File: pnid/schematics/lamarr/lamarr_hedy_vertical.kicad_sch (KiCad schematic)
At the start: 103 parts, among them U1 Rocket_Big

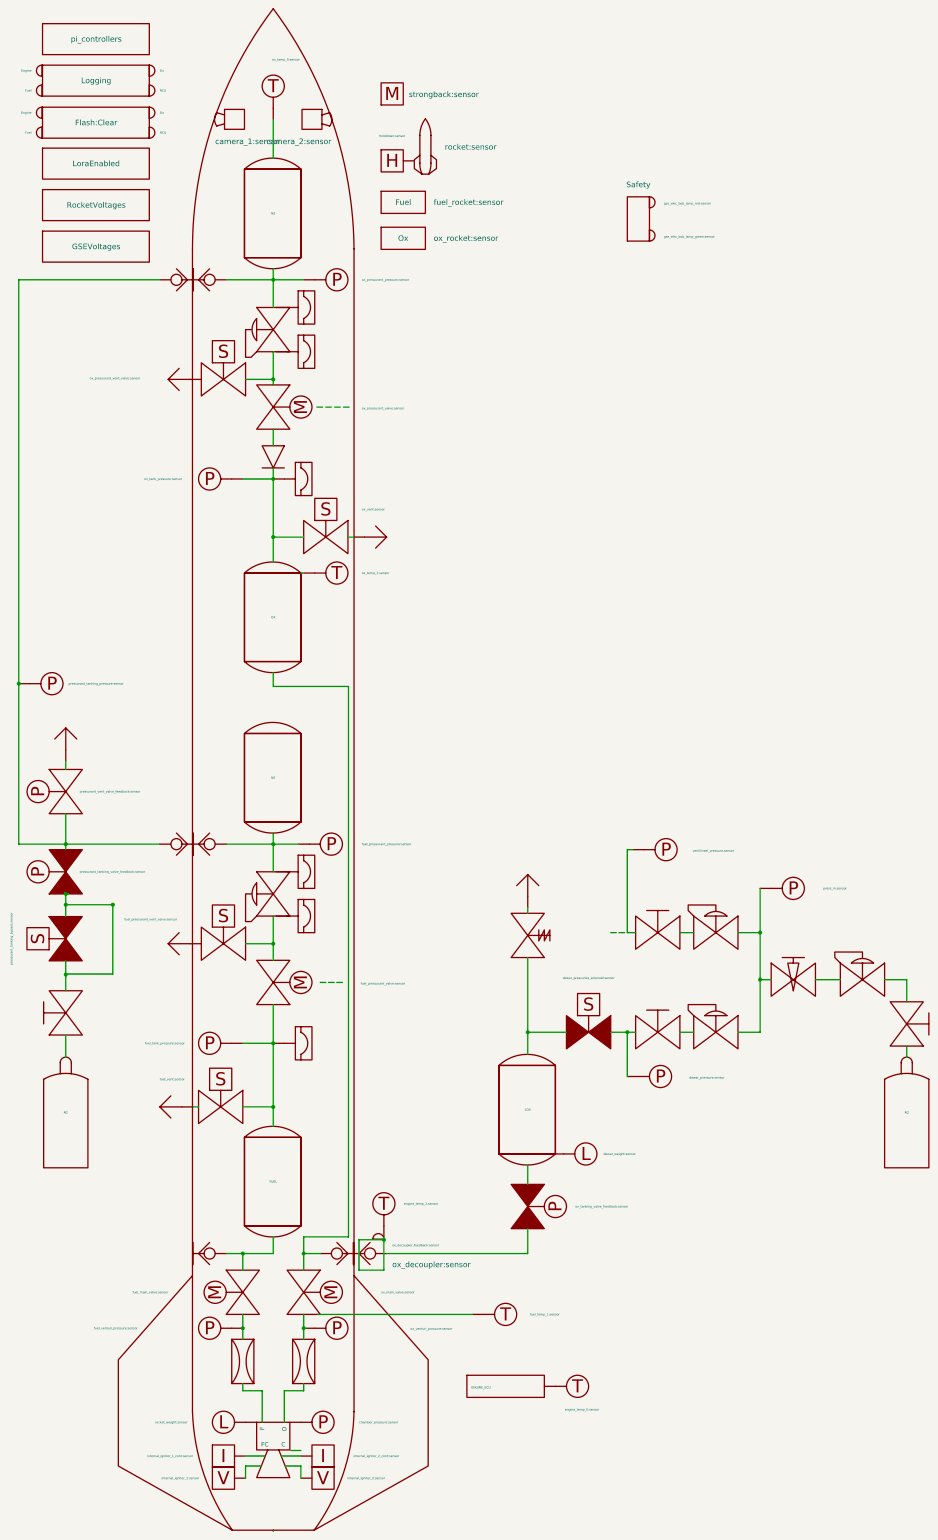
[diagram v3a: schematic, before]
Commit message: optimize pnid label positions
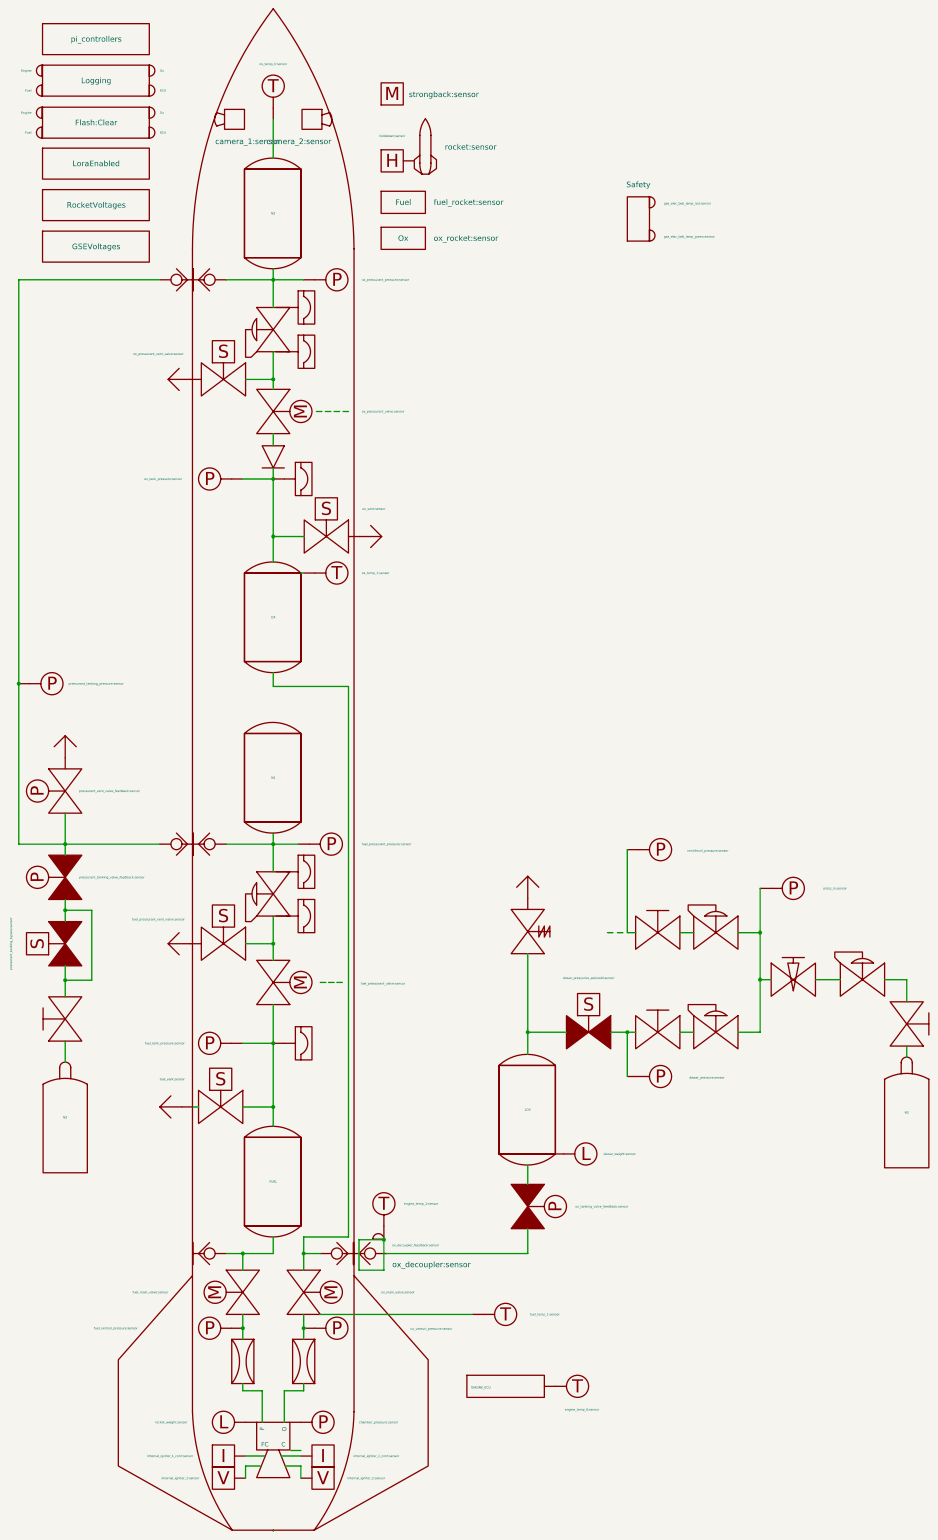
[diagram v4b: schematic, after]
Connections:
- net at engine.~ (C): now also venturi1.~
- net at ox_venturi.~: now also ox_main_valve.~, ox_venturi_pressure.~; no longer engine.~ (C)
- net at venturi1.~: now also fuel_main_valve.~, fuel_venturi_pressure.~; no longer engine.~ (C)
- net at dewar_needle_valve?.~: now also C2.~, C3.~, press_in.~; no longer C1.~
- new net: engine.~ (C), ox_venturi.~
- new net: OX.~, ox_main_valve.~, ox_quick_connect.~
- new net: DewarOverPressureValve?.~, LOX.~, dewar_pressurize_solenoid.~
- new net: C1.~, dewar_needle_valve?.~
- new net: ox_pressurant_valve.~, ox_pressurant_vent_valve.~, pressurantPressureRegulator2.~
- new net: FUEL.~, fuel_main_valve.~, ox_quick_connect1.~
- new net: fuel_pressurant_valve.~, fuel_pressurant_vent_valve.~, pressurantPressureRegulator1.~
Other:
- moved on the sheet: N2

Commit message: label position again
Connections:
- net at engine.~ (C): now also venturi1.~
- net at ox_venturi.~: now also ox_main_valve.~, ox_venturi_pressure.~; no longer engine.~ (C)
- net at venturi1.~: now also fuel_main_valve.~, fuel_venturi_pressure.~; no longer engine.~ (C)
- net at dewar_needle_valve?.~: now also C2.~, C3.~, press_in.~; no longer C1.~
- new net: engine.~ (C), ox_venturi.~
- new net: OX.~, ox_main_valve.~, ox_quick_connect.~
- new net: DewarOverPressureValve?.~, LOX.~, dewar_pressurize_solenoid.~
- new net: C1.~, dewar_needle_valve?.~
- new net: ox_pressurant_valve.~, ox_pressurant_vent_valve.~, pressurantPressureRegulator2.~
- new net: FUEL.~, fuel_main_valve.~, ox_quick_connect1.~
- new net: fuel_pressurant_valve.~, fuel_pressurant_vent_valve.~, pressurantPressureRegulator1.~
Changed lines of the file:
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@@
 		)
 		(property "Value" "fuel_pressurant_valve:sensor"
-			(at 87.376 71.374 90)
+			(at 87.376 71.12 90)
 			(effects
 				(font

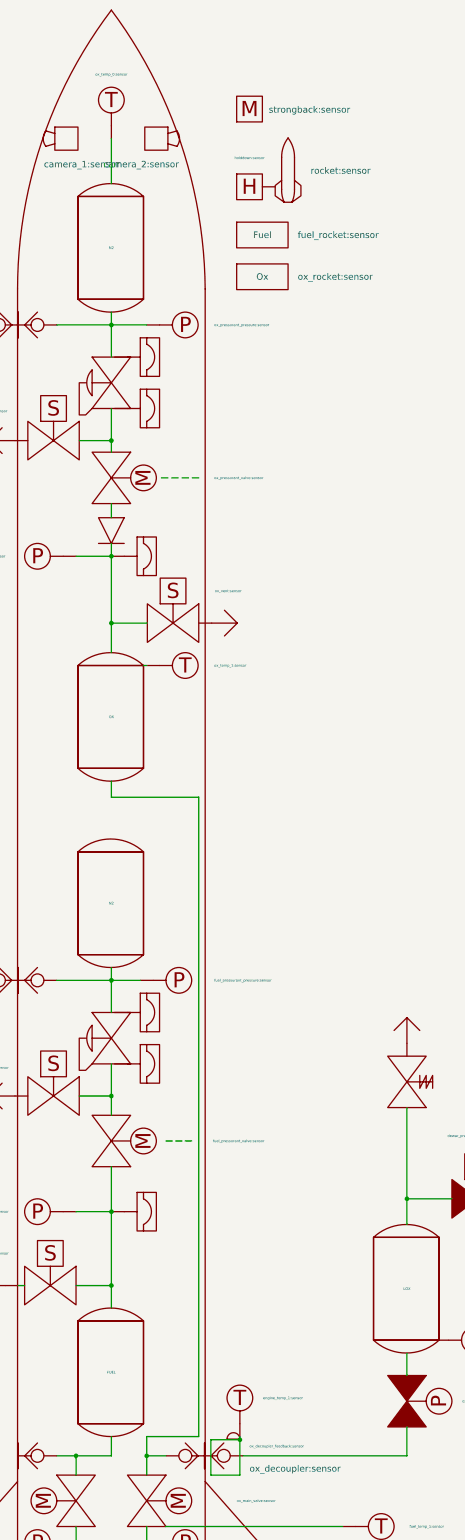
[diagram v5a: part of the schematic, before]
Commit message: update retract & charging pnid elements
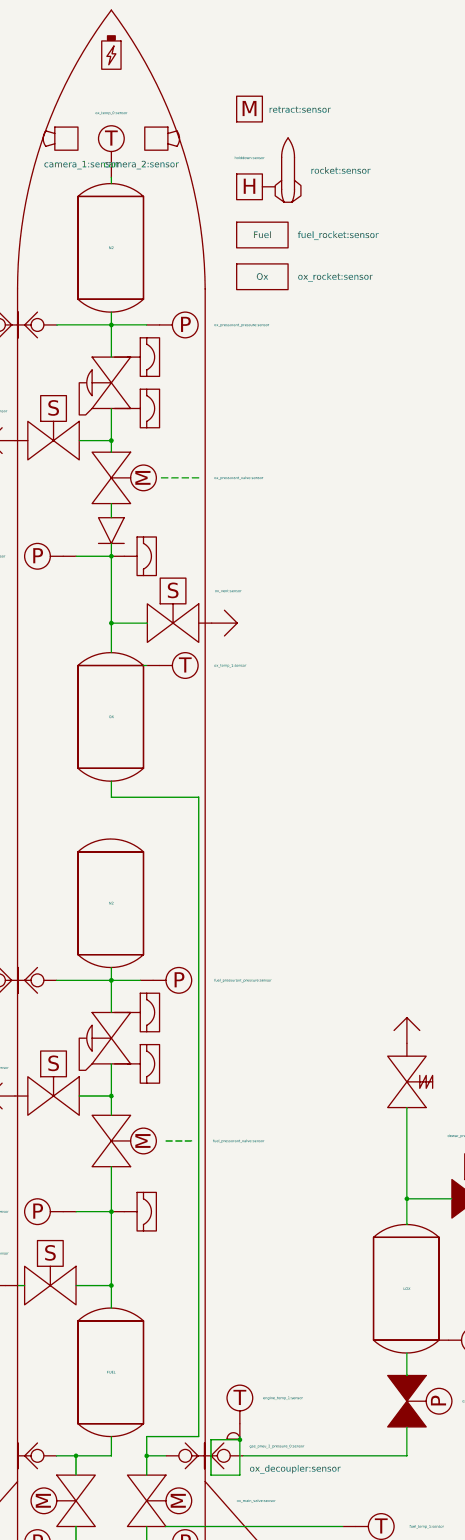
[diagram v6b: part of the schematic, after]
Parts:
- added U2: gse_elec_bob_igniter_2:sensor, symbol PnID-Lib:Battery
- Motor1: value strongback:sensor -> retract:sensor
- ox_decoupler_feedback: value ox_decoupler_feedback:sensor -> gse_pneu_2_pressure_0:sensor
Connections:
- net at engine.~ (C): now also venturi1.~
- net at ox_venturi.~: now also ox_main_valve.~, ox_venturi_pressure.~; no longer engine.~ (C)
- net at venturi1.~: now also fuel_main_valve.~, fuel_venturi_pressure.~; no longer engine.~ (C)
- net at dewar_needle_valve?.~: now also C2.~, C3.~, press_in.~; no longer C1.~
- new net: engine.~ (C), ox_venturi.~
- new net: OX.~, ox_main_valve.~, ox_quick_connect.~
- new net: DewarOverPressureValve?.~, LOX.~, dewar_pressurize_solenoid.~
- new net: C1.~, dewar_needle_valve?.~
- new net: ox_pressurant_valve.~, ox_pressurant_vent_valve.~, pressurantPressureRegulator2.~
- new net: FUEL.~, fuel_main_valve.~, ox_quick_connect1.~
- new net: fuel_pressurant_valve.~, fuel_pressurant_vent_valve.~, pressurantPressureRegulator1.~
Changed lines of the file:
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@@
 	(wire
 		(pts
-			(xy 67.31 -127) (xy 67.31 -118.11)
+			(xy 67.31 -119.38) (xy 67.31 -118.11)
 		)
 		(stroke
@@
 		(lib_name "Sensor_Temperature_2")
 		(lib_id "PnID-Lib:Sensor_Temperature")
-		(at 67.31 -134.62 0)
+		(at 67.31 -127 0)
 		(unit 1)
 		(exclude_from_sim no)
@@
 		(dnp no)
 		(property "Reference" "ox_decoupler_temperature1"
-			(at 62.357 -141.097 0)
+			(at 62.357 -133.477 0)
 			(effects
 				(font
@@
 		)
 		(property "Value" "ox_temp_0:sensor"
-			(at 67.31 -139.7 0)
+			(at 67.31 -132.08 0)
 			(effects
 				(font
@@
 		)
 		(property "Footprint" ""
-			(at 67.31 -134.62 0)
+			(at 67.31 -127 0)
 			(effects
 				(font
@@
 		)
 		(property "Datasheet" ""
-			(at 67.31 -134.62 0)
+			(at 67.31 -127 0)
 			(effects
 				(font
@@
 		)
 		(property "Description" ""
-			(at 67.31 -134.62 0)
+			(at 67.31 -127 0)
 			(effects
 				(font
@@
 		)
 		(property "Unit" "˚C"
-			(at 67.31 -134.62 0)
+			(at 67.31 -127 0)
 			(effects
 				(font
@@
 		)
 		(property "Action_Reference" " "
-			(at 67.31 -134.62 0)
+			(at 67.31 -127 0)
 			(effects
 				(font
@@
 	)
 	(symbol
+		(lib_id "PnID-Lib:Battery")
+		(at 67.31 -143.51 0)
+		(unit 1)
+		(exclude_from_sim no)
+		(in_bom yes)
+		(on_board yes)
+		(dnp no)
+		(property "Reference" "U2"
+			(at 67.31 -150.876 0)
+			(effects
+				(font
+					(size 1.27 1.27)
+				)
+				(hide yes)
+			)
+		)
+		(property "Value" "gse_elec_bob_igniter_2:sensor"
+			(at 67.31 -137.16 0)
+			(effects
+				(font
+					(size 1.27 1.27)
+				)
+				(hide yes)
+			)
+		)
+		(property "Footprint" ""
+			(at 67.691 -143.51 0)
+			(effects
+				(font
+					(size 1.27 1.27)
+				)
+				(hide yes)
+			)
+		)
+		(property "Datasheet" ""
+			(at 67.691 -143.51 0)
+			(effects
+				(font
+					(size 1.27 1.27)
+				)
+				(hide yes)
+			)
+		)
+		(property "Description" ""
+			(at 67.31 -143.51 0)
+			(effects
+				(font
+					(size 1.27 1.27)
+				)
+				(hide yes)
+			)
+		)
+		(property "Unit" "V"
+			(at 67.31 -143.51 0)
+			(effects
+				(font
+					(size 1.27 1.27)
+				)
+				(hide yes)
+			)
+		)
+		(instances
+			(project ""
+				(path "/604fc9f3-63a6-4133-afd1-4a5c2507dc1d"
+					(reference "U2")
+					(unit 1)
+				)
+			)
+		)
+	)
+	(symbol
 		(lib_id "PnID-Lib:PressureRegulator")
 		(at 67.31 -78.74 90)
@@
 			)
 		)
-		(property "Value" "strongback:sensor"
+		(property "Value" "retract:sensor"
 			(at 98.425 -132.715 0)
 			(effects
@@
 			)
 		)
-		(property "Value" "ox_decoupler_feedback:sensor"
+		(property "Value" "gse_pneu_2_pressure_0:sensor"
 			(at 94.615 131.445 0)
 			(effects

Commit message: remove holddown sensor. we dont use it anymore
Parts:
- removed Holddown: holddown:sensor, symbol PnID-Lib:heater
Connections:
- net at engine.~ (C): now also venturi1.~
- net at ox_venturi.~: now also ox_main_valve.~, ox_venturi_pressure.~; no longer engine.~ (C)
- net at venturi1.~: now also fuel_main_valve.~, fuel_venturi_pressure.~; no longer engine.~ (C)
- net at dewar_needle_valve?.~: now also C2.~, C3.~, press_in.~; no longer C1.~
- new net: engine.~ (C), ox_venturi.~
- new net: OX.~, ox_main_valve.~, ox_quick_connect.~
- new net: DewarOverPressureValve?.~, LOX.~, dewar_pressurize_solenoid.~
- new net: C1.~, dewar_needle_valve?.~
- new net: ox_pressurant_valve.~, ox_pressurant_vent_valve.~, pressurantPressureRegulator2.~
- new net: FUEL.~, fuel_main_valve.~, ox_quick_connect1.~
- new net: fuel_pressurant_valve.~, fuel_pressurant_vent_valve.~, pressurantPressureRegulator1.~
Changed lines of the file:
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@@
-	)
-	(symbol
-		(lib_id "PnID-Lib:heater")
-		(at 94.615 -117.475 0)
-		(unit 1)
-		(exclude_from_sim no)
-		(in_bom yes)
-		(on_board yes)
-		(dnp no)
-		(property "Reference" "Holddown"
-			(at 89.535 -119.761 0)
-			(effects
-				(font
-					(size 0.508 0.508)
-				)
-				(hide yes)
-			)
-		)
-		(property "Value" "holddown:sensor"
-			(at 94.615 -123.19 0)
-			(effects
-				(font
-					(size 0.508 0.508)
-				)
-			)
-		)
-		(property "Footprint" ""
-			(at 94.615 -117.475 0)
-			(effects
-				(font
-					(size 1.27 1.27)
-				)
-				(hide yes)
-			)
-		)
-		(property "Datasheet" ""
-			(at 94.615 -117.475 0)
-			(effects
-				(font
-					(size 1.27 1.27)
-				)
-				(hide yes)
-			)
-		)
-		(property "Description" "A"
-			(at 94.615 -117.475 0)
-			(effects
-				(font
-					(size 1.27 1.27)
-				)
-				(hide yes)
-			)
-		)
-		(pin "~"
-		)
-		(instances
-			(project "lamarr_hedy_vertical"
-				(path "/604fc9f3-63a6-4133-afd1-4a5c2507dc1d"
-					(reference "Holddown")
-					(unit 1)
-				)
-			)
-		)
 	)
 	(symbol
@@
 	(symbol
 		(lib_id "PnID-Lib:Rocket_Channel")
-		(at 102.235 -118.745 0)
+		(at 94.615 -118.745 0)
 		(unit 1)
 		(exclude_from_sim no)
@@
 		(dnp no)
 		(property "Reference" "R1"
-			(at 106.299 -125.8571 0)
+			(at 98.679 -125.8571 0)
 			(effects
 				(font
@@
 		)
 		(property "Value" "rocket:sensor"
-			(at 106.68 -120.65 0)
-			(effects
-				(font
-					(size 1.27 1.27)
-				)
-				(justify left)
-			)
-		)
-		(property "Footprint" ""
-			(at 102.235 -115.697 0)
-			(effects
-				(font
-					(size 1.27 1.27)
-				)
-				(hide yes)
-			)
-		)
-		(property "Datasheet" ""
-			(at 102.235 -115.697 0)
-			(effects
-				(font
-					(size 1.27 1.27)
-				)
-				(hide yes)
-			)
-		)
-		(property "Description" ""
-			(at 102.235 -118.745 0)
+			(at 99.06 -120.65 0)
+			(effects
+				(font
+					(size 1.27 1.27)
+				)
+				(justify left)
+			)
+		)
+		(property "Footprint" ""
+			(at 94.615 -115.697 0)
+			(effects
+				(font
+					(size 1.27 1.27)
+				)
+				(hide yes)
+			)
+		)
+		(property "Datasheet" ""
+			(at 94.615 -115.697 0)
+			(effects
+				(font
+					(size 1.27 1.27)
+				)
+				(hide yes)
+			)
+		)
+		(property "Description" ""
+			(at 94.615 -118.745 0)
 			(effects
 				(font
@@
 		)
 		(property "Unit" " "
-			(at 106.299 -120.7771 0)
+			(at 98.679 -120.7771 0)
 			(effects
 				(font
@@
 		)
 		(property "Action_Reference" " "
-			(at 106.299 -118.2371 0)
+			(at 98.679 -118.2371 0)
 			(effects
 				(font
@@
 		)
 		(property "Data_Content" " "
-			(at 106.299 -115.6971 0)
-			(effects
-				(font
+			(at 98.679 -115.6971 0)
+			(effects
+				(font

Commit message: improve feedback for battery
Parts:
- U2: value gse_elec_bob_igniter_2:sensor -> ox_sense_12V:sensor
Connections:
- net at engine.~ (C): now also venturi1.~
- net at ox_venturi.~: now also ox_main_valve.~, ox_venturi_pressure.~; no longer engine.~ (C)
- net at venturi1.~: now also fuel_main_valve.~, fuel_venturi_pressure.~; no longer engine.~ (C)
- net at dewar_needle_valve?.~: now also C2.~, C3.~, press_in.~; no longer C1.~
- new net: engine.~ (C), ox_venturi.~
- new net: OX.~, ox_main_valve.~, ox_quick_connect.~
- new net: DewarOverPressureValve?.~, LOX.~, dewar_pressurize_solenoid.~
- new net: C1.~, dewar_needle_valve?.~
- new net: ox_pressurant_valve.~, ox_pressurant_vent_valve.~, pressurantPressureRegulator2.~
- new net: FUEL.~, fuel_main_valve.~, ox_quick_connect1.~
- new net: fuel_pressurant_valve.~, fuel_pressurant_vent_valve.~, pressurantPressureRegulator1.~
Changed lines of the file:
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@@
 			)
 		)
-		(property "Value" "gse_elec_bob_igniter_2:sensor"
+		(property "Value" "ox_sense_12V:sensor"
 			(at 67.31 -137.16 0)
 			(effects
@@
 					(size 1.27 1.27)
 				)
-				(hide yes)
 			)
 		)
